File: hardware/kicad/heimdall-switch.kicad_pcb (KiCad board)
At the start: 2 copper layers, 63.5 x 23 mm, 42 parts, among them J1 SWD (ARM 10-pin), J2 LOAD_OUT, J3 BATT_IN, J4 B3B-XH-A, Q1 AO3400A, Q2 BSS84, Q3 AO4407A, Q4 AO4407A, Q5 AO3400A, Q6 BSS84, SW1 PTS810, U1 BT832, U2 TPS629206, Y1 32.768kHz

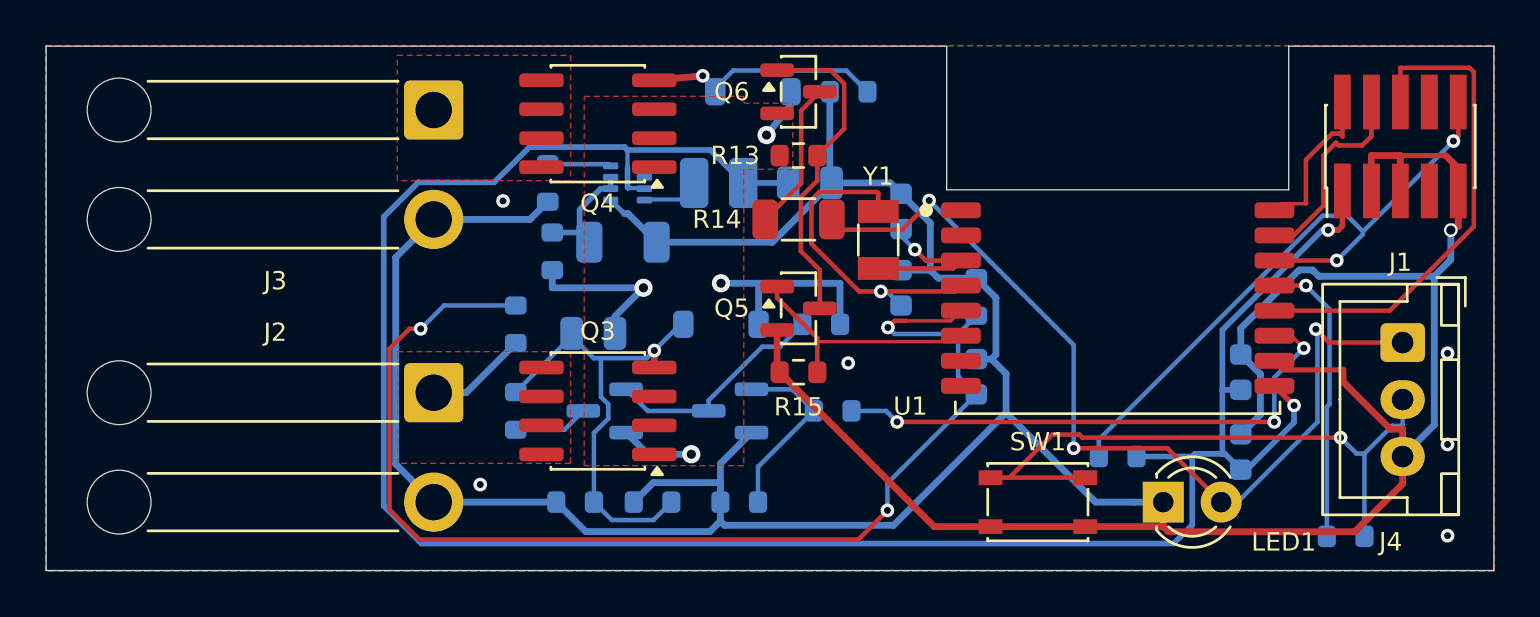
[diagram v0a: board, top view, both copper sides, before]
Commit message: J1: Tag-Connect TC2030-NL in place of the 2x5 SWD header
The Samtec FTSH-105 cost $1.46/board for a connector used once per
board (to flash the DFU bootloader). The TC2030-NL footprint is pads
plus three locating holes, no part; the TC2030-CTX-NL cable ends in the
same ARM 10-pin socket the probes use. No-legs variant so nothing goes
through to the populated bottom side.

Schematic: J1 symbol swapped to Conn_ARM_SWD_TagConnect_TC2030-NL,
labels rewired, excluded from BOM. PCB: footprint in J1's old spot,
SWD nets re-routed with everything else locked (rotation 0 of four
tried), +3V3 to pad 1 hand-routed. ERC/DRC clean, full parity.

Co-Authored-By: Claude Opus 5.5 <noreply@anthropic.com>
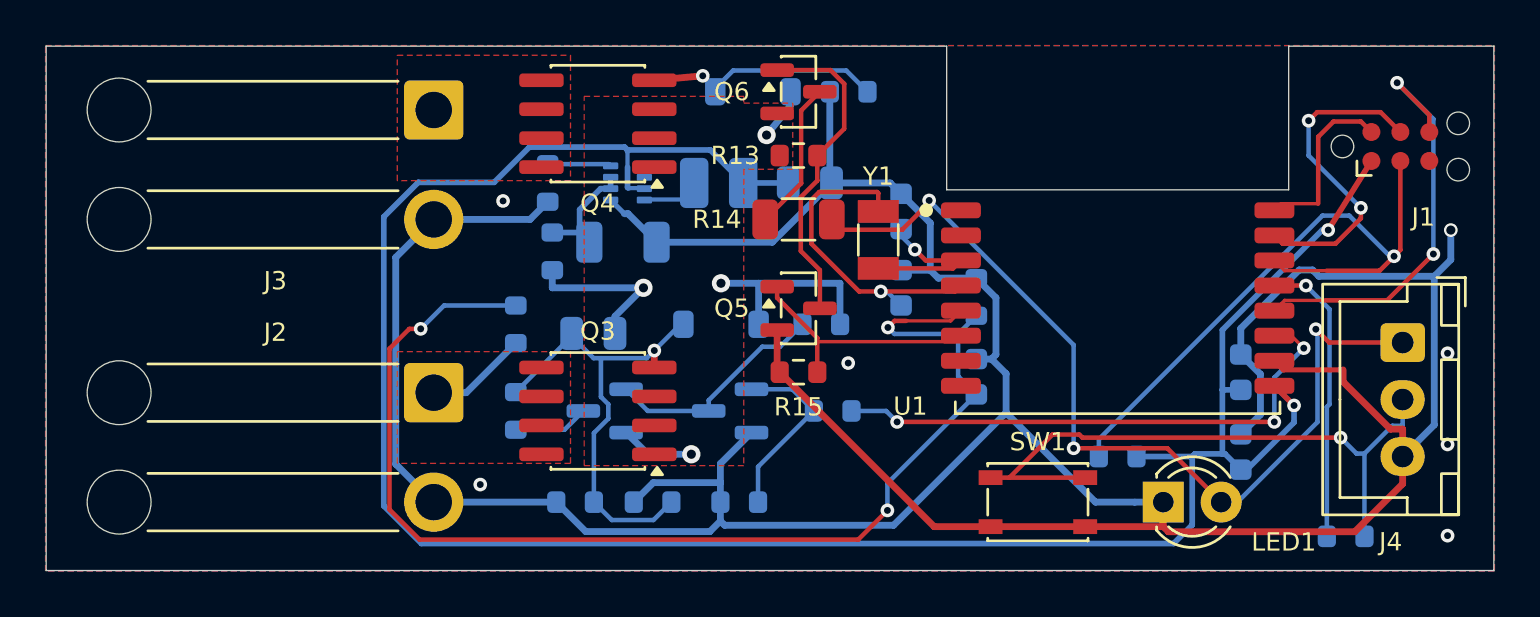
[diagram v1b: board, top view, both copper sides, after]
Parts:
- J1: value SWD (ARM 10-pin) -> TC2030-NL (SWD); footprint Connector_PinHeader_1.27mm:PinHeader_2x05_P1.27mm_Vertical_SMD -> Connector:Tag-Connect_TC2030-IDC-NL_2x03_P1.27mm_Vertical
- turned J1 to 0 degrees
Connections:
- J1 pad 3: GND -> /nRESET
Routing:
- net GND: track 177.1 -> 167.1 mm
- net /SWDCLK: track 8.95 -> 14.2 mm, vias 0 -> 2
- net /SWO: track 21.9 -> 18.9 mm, vias 0 -> 2
- net +3V3: track 99.2 -> 100.6 mm
- net /SWDIO: track 7.06 -> 7.78 mm
- net /nRESET: track 28.6 -> 28.5 mm, vias 2 -> 1
